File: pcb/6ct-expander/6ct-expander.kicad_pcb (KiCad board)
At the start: 2 copper layers, 88 x 30 mm, 57 parts, among them J1 SJ-3524-SMT-TR, J2 SJ-3524-SMT-TR, J3 SJ-3524-SMT-TR, J4 SJ-3524-SMT-TR, J5 SJ-3524-SMT-TR, J6 SJ-3524-SMT-TR, J7 Conn_02x05_Odd_Even

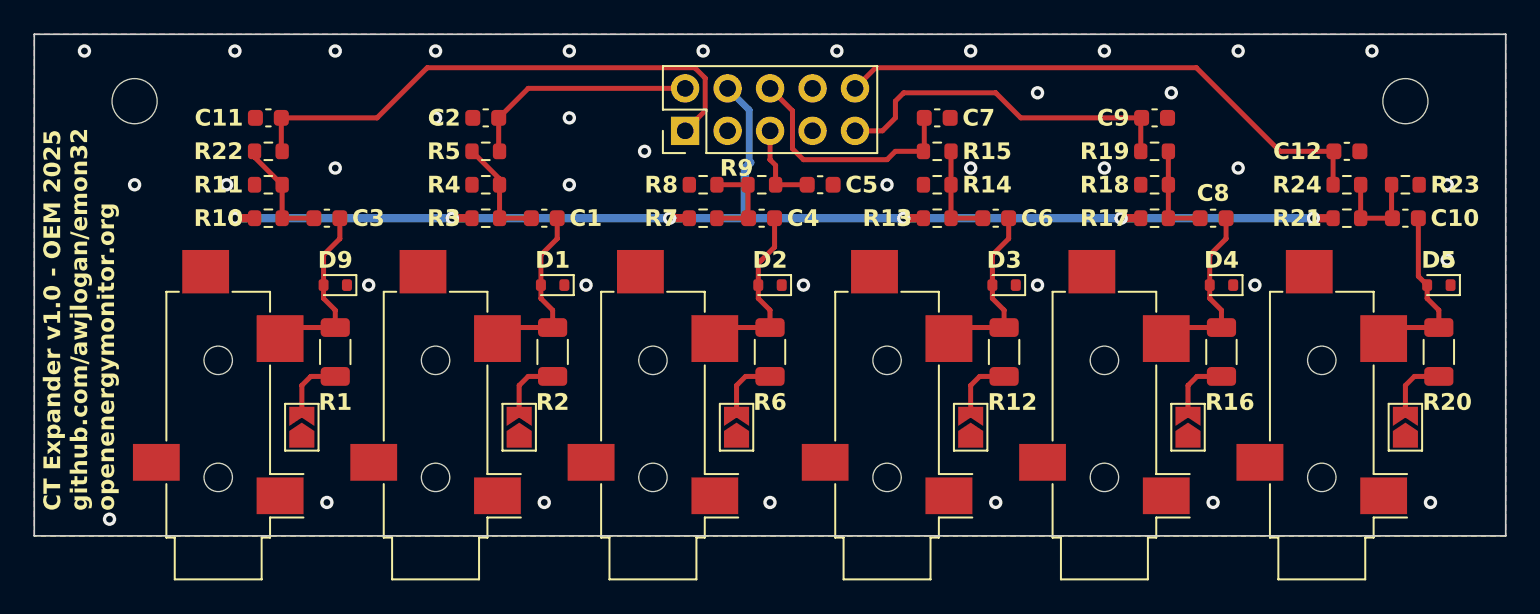
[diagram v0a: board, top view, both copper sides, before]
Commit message: [6CT] Mirror connector pins to match emonPi3 pin out
  - Mirrored to emonPi3 pin out facing *down*
  - Also update board information
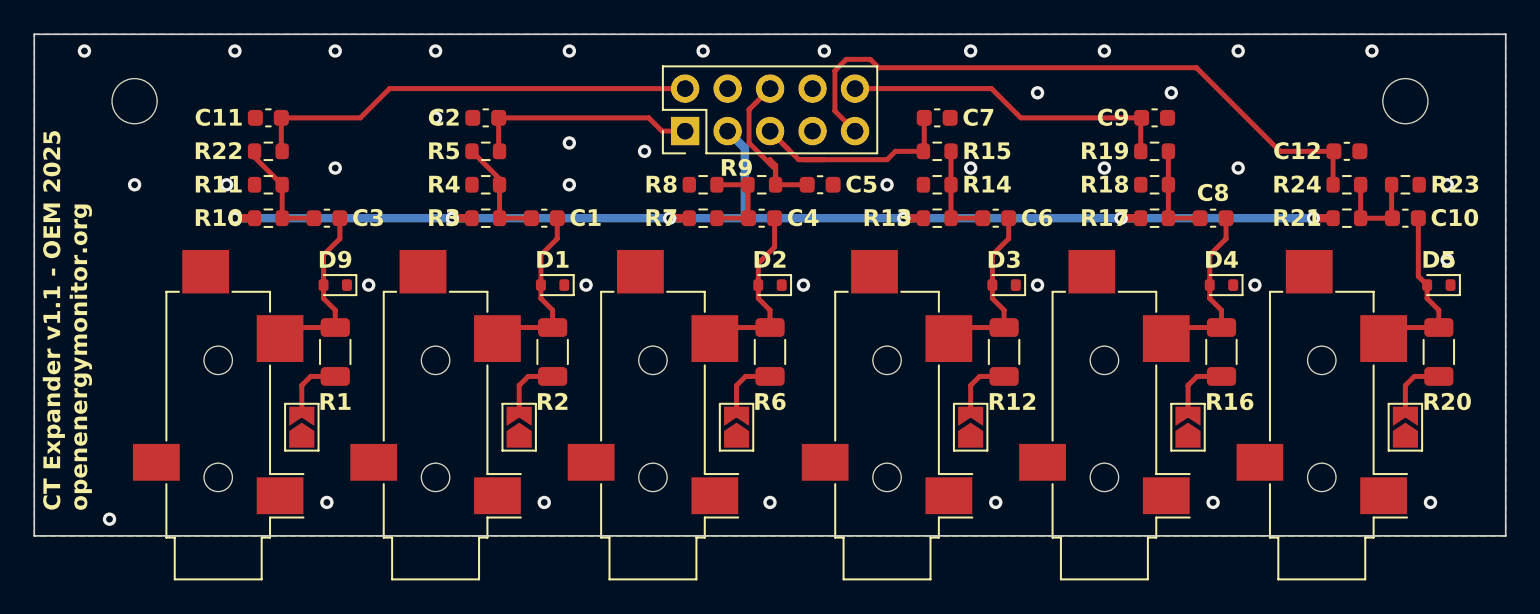
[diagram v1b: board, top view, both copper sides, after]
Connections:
- J7 pad 1: /CT7 -> /CT8
- J7 pad 10: /CT12 -> /CT11
- J7 pad 2: /CT8 -> /CT7
- J7 pad 3: GND -> /V_{REF}
- J7 pad 4: /V_{REF} -> GND
- J7 pad 5: /CT9 -> /CT10
- J7 pad 6: /CT10 -> /CT9
- J7 pad 7: unconnected-(J7-Pin_7-Pad7) -> GND
- J7 pad 8: GND -> unconnected-(J7-Pin_8-Pad8)
- J7 pad 9: /CT11 -> /CT12
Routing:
- net /CT7: track 32.4 -> 26.8 mm
- net /CT12: track 33.2 -> 38.5 mm
- net /CT9: track 5.26 -> 10.5 mm
- net /V_{REF}: track 80.4 -> 77.2 mm
- net /CT11: track 21.2 -> 19.8 mm
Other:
- board text added: "CT Expander v1.1 - OEM 2025 openenergymonitor.org"
- board text removed: "CT Expander v1.0 - OEM 2025 github.com/awjlogan/emon32 openenergymonitor.org"
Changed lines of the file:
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@@
 	(net 25 "unconnected-(J6-PadR)")
 	(net 26 "/V_{REF}")
-	(net 27 "unconnected-(J7-Pin_7-Pad7)")
+	(net 27 "unconnected-(J7-Pin_8-Pad8)")
 	(net 28 "Net-(JP1-B)")
 	(net 29 "Net-(JP2-B)")
@@
 		(locked yes)
 		(layer "F.Cu")
-		(at 138.925 105.775 90)
+		(at 138.925 105.79 90)
 		(descr "Through hole straight pin header, 2x05, 2.54mm pitch, double rows")
 		(tags "Through hole pin header THT 2x05 2.54mm double row")
@@
 		)
 		(fp_text user "${REFERENCE}"
-			(at 1.27 5.08 0)
+			(at -1 -2.925 0)
 			(layer "F.Fab")
 			(effects
@@
 			(layers "*.Cu" "*.Mask")
 			(remove_unused_layers no)
-			(net 18 "/CT7")
+			(net 3 "/CT8")
 			(pinfunction "Pin_1")
 			(pintype "passive")
@@
 			(layers "*.Cu" "*.Mask")
 			(remove_unused_layers no)
-			(net 3 "/CT8")
+			(net 18 "/CT7")
 			(pinfunction "Pin_2")
 			(pintype "passive")
@@
 			(layers "*.Cu" "*.Mask")
 			(remove_unused_layers no)
-			(net 4 "GND")
+			(net 26 "/V_{REF}")
 			(pinfunction "Pin_3")
 			(pintype "passive")
@@
 			(layers "*.Cu" "*.Mask")
 			(remove_unused_layers no)
-			(net 26 "/V_{REF}")
+			(net 4 "GND")
 			(pinfunction "Pin_4")
 			(pintype "passive")
@@
 			(layers "*.Cu" "*.Mask")
 			(remove_unused_layers no)
-			(net 9 "/CT9")
+			(net 12 "/CT10")
 			(pinfunction "Pin_5")
 			(pintype "passive")
@@
 			(layers "*.Cu" "*.Mask")
 			(remove_unused_layers no)
-			(net 12 "/CT10")
+			(net 9 "/CT9")
 			(pinfunction "Pin_6")
 			(pintype "passive")
@@
 			(layers "*.Cu" "*.Mask")
 			(remove_unused_layers no)
-			(net 27 "unconnected-(J7-Pin_7-Pad7)")
+			(net 4 "GND")
 			(pinfunction "Pin_7")
-			(pintype "passive+no_connect")
+			(pintype "passive")
 		)
 		(pad "8" thru_hole oval
@@
 			(layers "*.Cu" "*.Mask")
 			(remove_unused_layers no)
-			(net 4 "GND")
+			(net 27 "unconnected-(J7-Pin_8-Pad8)")
 			(pinfunction "Pin_8")
-			(pintype "passive")
+			(pintype "passive+no_connect")
 		)
 		(pad "9" thru_hole oval
@@
 			(layers "*.Cu" "*.Mask")
 			(remove_unused_layers no)
-			(net 15 "/CT11")
+			(net 19 "/CT12")
 			(pinfunction "Pin_9")
 			(pintype "passive")
@@
 			(layers "*.Cu" "*.Mask")
 			(remove_unused_layers no)
-			(net 19 "/CT12")
+			(net 15 "/CT11")
 			(pinfunction "Pin_10")
 			(pintype "passive")
@@
 		(layer "Edge.Cuts")
 	)
-	(gr_text "CT Expander v1.0 - OEM 2025\ngithub.com/awjlogan/emon32\nopenenergymonitor.org"
+	(gr_text "CT Expander v1.1 - OEM 2025\nopenenergymonitor.org"
 		(at 100.5 128.5 90)
 		(layer "F.SilkS")
@@
 	)
 	(segment
-		(start 129.54 103.235)
-		(end 127.775 105)
+		(start 137.54 105.79)
+		(end 136.75 105)
+		(width 0.3)
+		(layer "F.Cu")
+		(net 3)
+	)
+	(segment
+		(start 127.775 105)
+		(end 136.75 105)
 		(width 0.3)
 		(layer "F.Cu")
@@
 	)
 	(segment
-		(start 138.925 103.235)
-		(end 129.54 103.235)
+		(start 138.925 105.79)
+		(end 137.54 105.79)
 		(width 0.3)
 		(layer "F.Cu")
@@
 	)
 	(via
-		(at 132 105)
+		(at 132 106.5)
 		(size 0.8)
 		(drill 0.4)
@@
 	)
 	(via
-		(at 148 101)
+		(at 147.25 101)
 		(size 0.8)
 		(drill 0.4)
@@
 	)
 	(segment
+		(start 142.755 104.5)
+		(end 144.005 103.25)
+		(width 0.3)
+		(layer "F.Cu")
+		(net 9)
+	)
+	(segment
+		(start 144.335 108.085)
+		(end 142.75 106.5)
+		(width 0.3)
+		(layer "F.Cu")
+		(net 9)
+	)
+	(segment
 		(start 144.335 109)
 		(end 144.335 107.835)
@@
 	)
 	(segment
-		(start 144.005 107.495)
-		(end 144.005 105.775)
+		(start 142.75 106.5)
+		(end 142.75 104.5)
+		(width 0.3)
+		(layer "F.Cu")
+		(net 9)
+	)
+	(segment
+		(start 144.335 109)
+		(end 144.335 108.085)
 		(width 0.3)
 		(layer "F.Cu")
@@
 	)
 	(segment
+		(start 142.75 104.5)
+		(end 142.755 104.5)
+		(width 0.3)
+		(layer "F.Cu")
+		(net 9)
+	)
+	(segment
 		(start 144 107.5)
 		(end 144.005 107.495)
@@
 	)
 	(segment
-		(start 145.345 104.575)
-		(end 144.005 103.235)
+		(start 147.25 107.5)
+		(end 146 107.5)
 		(width 0.3)
 		(layer "F.Cu")
@@
 	)
 	(segment
-		(start 146 107.5)
-		(end 145.345 106.845)
+		(start 145.06 106.845)
+		(end 144.005 105.79)
 		(width 0.3)
 		(layer "F.Cu")
@@
 	)
 	(segment
-		(start 145.345 106.845)
-		(end 145.345 104.575)
+		(start 151 107.5)
+		(end 147.25 107.5)
 		(width 0.3)
 		(layer "F.Cu")
@@
 	)
 	(segment
-		(start 151 107.5)
-		(end 146 107.5)
+		(start 147.25 107.5)
+		(end 145.715 107.5)
+		(width 0.3)
+		(layer "F.Cu")
+		(net 12)
+	)
+	(segment
+		(start 145.715 107.5)
+		(end 144.005 105.79)
 		(width 0.3)
 		(layer "F.Cu")
@@
 	)
 	(segment
-		(start 151.5 105)
-		(end 150.725 105.775)
-		(width 0.3)
-		(layer "F.Cu")
-		(net 15)
-	)
-	(segment
-		(start 150.725 105.775)
-		(end 149.085 105.775)
-		(width 0.3)
-		(layer "F.Cu")
-		(net 15)
-	)
-	(segment
 		(start 159 105)
-		(end 157.5 103.5)
+		(end 158.75 104.75)
 		(width 0.3)
 		(layer "F.Cu")
@@
 	)
 	(segment
-		(start 157.5 103.5)
-		(end 152 103.5)
-		(width 0.3)
-		(layer "F.Cu")
-		(net 15)
-	)
-	(segment
-		(start 152 103.5)
-		(end 151.5 104)
+		(start 158.75 104.75)
+		(end 157.25 103.25)
 		(width 0.3)
 		(layer "F.Cu")
@@
 	)
 	(segment
-		(start 151.5 104)
-		(end 151.5 105)
+		(start 157.25 103.25)
+		(end 149.085 103.25)
 		(width 0.3)
 		(layer "F.Cu")
@@
 	(segment
 		(start 114.775 105)
-		(end 120.5 105)
+		(end 119.5 105)
 		(width 0.3)
 		(layer "F.Cu")
@@
 	)
 	(segment
-		(start 140.125 102.625)
-		(end 140.125 104.575)
+		(start 121.25 103.25)
+		(end 138.925 103.25)
 		(width 0.3)
 		(layer "F.Cu")
@@
 	)
 	(segment
-		(start 139.5 102)
-		(end 140.125 102.625)
+		(start 119.5 105)
+		(end 121.25 103.25)
 		(width 0.3)
 		(layer "F.Cu")
@@
 	)
 	(segment
-		(start 120.5 105)
-		(end 123.5 102)
+		(start 114.775 105)
+		(end 114.775 106.95)
 		(width 0.3)
 		(layer "F.Cu")
@@
 	)
 	(segment
-		(start 123.5 102)
-		(end 139.5 102)
+		(start 177.675 109)
+		(end 177.675 107.05)
 		(width 0.3)
 		(layer "F.Cu")
-		(net 18)
+		(net 19)
 	)
 	(segment
-		(start 114.775 105)
-		(end 114.775 106.95)
+		(start 177.725 107)
+		(end 174.5 107)
 		(width 0.3)
 		(layer "F.Cu")
-		(net 18)
+		(net 19)
 	)
 	(segment
-		(start 140.125 104.575)
-		(end 138.925 105.775)
+		(start 148.562075 101.5)
+		(end 147.884 102.178075)
 		(width 0.3)
 		(layer "F.Cu")
-		(net 18)
+		(net 19)
 	)
 	(segment
-		(start 174.5 107)
-		(end 169.5 102)
+		(start 169.5 102)
+		(end 150.5 102)
 		(width 0.3)
 		(layer "F.Cu")
@@
 	)
 	(segment
-		(start 177.675 109)
-		(end 177.675 107.05)
+		(start 150 101.5)
+		(end 148.562075 101.5)
 		(width 0.3)
 		(layer "F.Cu")
@@
 	)
 	(segment
-		(start 169.5 102)
-		(end 150.32 102)
+		(start 147.884 102.178075)
+		(end 147.884 104.589)
 		(width 0.3)
 		(layer "F.Cu")
@@
 	)
 	(segment
-		(start 177.725 107)
-		(end 174.5 107)
+		(start 150.5 102)
+		(end 150 101.5)
 		(width 0.3)
 		(layer "F.Cu")
@@
 	)
 	(segment
-		(start 150.32 102)
-		(end 149.085 103.235)
+		(start 174.5 107)
+		(end 169.5 102)
+		(width 0.3)
+		(layer "F.Cu")
+		(net 19)
+	)
+	(segment
+		(start 147.884 104.589)
+		(end 149.085 105.79)
 		(width 0.3)
 		(layer "F.Cu")
@@
 	)
 	(segment
-		(start 142.755 107.745)
-		(end 142.5 108)
-		(width 0.4)
-		(layer "B.Cu")
-		(net 26)
-	)
-	(segment
-		(start 142.83 107.67)
-		(end 142.5 108)
-		(width 0.5)
-		(layer "B.Cu")
-		(net 26)
-	)
-	(segment
 		(start 142.5 111)
 		(end 152 111)
@@
 	)
 	(segment
-		(start 142.755 104.525)
-		(end 142.755 107.745)
-		(width 0.4)
-		(layer "B.Cu")
-		(net 26)
-	)
-	(segment
 		(start 138 111)
 		(end 125 111)
@@
 	)
 	(segment
-		(start 141.465 103.235)
-		(end 142.755 104.525)
-		(width 0.4)
+		(start 141.465 105.79)
+		(end 142.5 106.825)
+		(width 0.5)
 		(layer "B.Cu")
 		(net 26)
@@
 	)
 	(segment
-		(start 142.5 108)
-		(end 142.5 111)
+		(start 152 111)
+		(end 165 111)
 		(width 0.5)
 		(layer "B.Cu")
@@
 	)
 	(segment
-		(start 152 111)
-		(end 165 111)
+		(start 142.5 106.825)
+		(end 142.5 111)
 		(width 0.5)
 		(layer "B.Cu")
